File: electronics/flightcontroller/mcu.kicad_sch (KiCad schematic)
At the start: 20 parts, among them J8 Micro_SD_Card_Det_CCON_CTF-11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, J9 SWD, SW1 SW_Push, U3 STM32L462CEUx, U6 GT-24-Mini

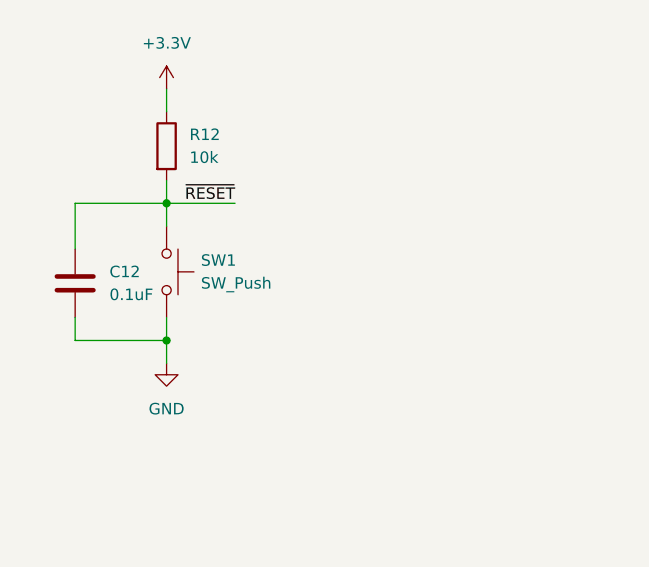
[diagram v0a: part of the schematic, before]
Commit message: electronics: Changed the 4V regulator and added some ordering codes.
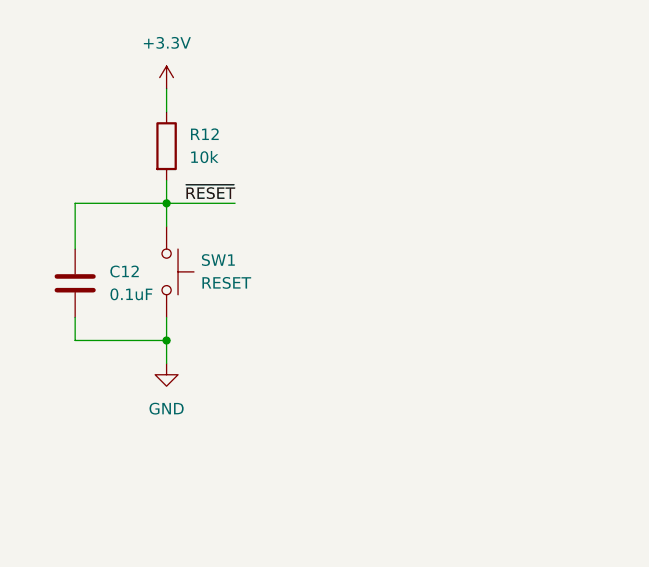
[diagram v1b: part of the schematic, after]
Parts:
- C11, C18, C19: Digikey (none) -> 490-GRM155R60J106ME05DCT-ND
- C12, C13, C14, C15, C16, C17: footprint (none) -> Capacitor_SMD:C_0402_1005Metric; Mouser (none) -> 81-GRM155R61H104KE4D
- SW1: value SW_Push -> RESET; Mouser (none) -> 611-KXT321LHS
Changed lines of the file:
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@@
+      (effects (font (size 1.27 1.27)) hide)
+    )
+    (property "Digikey" "490-GRM155R60J106ME05DCT-ND" (id 4) (at 19.05 179.07 0)
       (effects (font (size 1.27 1.27)) hide)
     )
@@
       (effects (font (size 1.27 1.27)) (justify left))
     )
-    (property "Footprint" "" (id 2) (at 22.5552 48.26 0)
+    (property "Footprint" "Capacitor_SMD:C_0402_1005Metric" (id 2) (at 22.5552 48.26 0)
       (effects (font (size 1.27 1.27)) hide)
     )
     (property "Datasheet" "~" (id 3) (at 21.59 44.45 0)
+      (effects (font (size 1.27 1.27)) hide)
+    )
+    (property "Mouser" "81-GRM155R61H104KE4D" (id 4) (at 21.59 44.45 0)
       (effects (font (size 1.27 1.27)) hide)
     )
@@
       (effects (font (size 1.27 1.27)) (justify left))
     )
-    (property "Footprint" "" (id 2) (at 204.1652 31.75 0)
+    (property "Footprint" "Capacitor_SMD:C_0402_1005Metric" (id 2) (at 204.1652 31.75 0)
       (effects (font (size 1.27 1.27)) hide)
     )
     (property "Datasheet" "~" (id 3) (at 203.2 27.94 0)
+      (effects (font (size 1.27 1.27)) hide)
+    )
+    (property "Mouser" "81-GRM155R61H104KE4D" (id 4) (at 203.2 27.94 0)
       (effects (font (size 1.27 1.27)) hide)
     )
@@
       (effects (font (size 1.27 1.27)) (justify left))
     )
-    (property "Footprint" "" (id 2) (at 216.8652 31.75 0)
+    (property "Footprint" "Capacitor_SMD:C_0402_1005Metric" (id 2) (at 216.8652 31.75 0)
       (effects (font (size 1.27 1.27)) hide)
     )
     (property "Datasheet" "~" (id 3) (at 215.9 27.94 0)
+      (effects (font (size 1.27 1.27)) hide)
+    )
+    (property "Mouser" "81-GRM155R61H104KE4D" (id 4) (at 215.9 27.94 0)
       (effects (font (size 1.27 1.27)) hide)
     )
@@
       (effects (font (size 1.27 1.27)) (justify left))
     )
-    (property "Footprint" "" (id 2) (at 229.5652 31.75 0)
+    (property "Footprint" "Capacitor_SMD:C_0402_1005Metric" (id 2) (at 229.5652 31.75 0)
       (effects (font (size 1.27 1.27)) hide)
     )
     (property "Datasheet" "~" (id 3) (at 228.6 27.94 0)
+      (effects (font (size 1.27 1.27)) hide)
+    )
+    (property "Mouser" "81-GRM155R61H104KE4D" (id 4) (at 228.6 27.94 0)
       (effects (font (size 1.27 1.27)) hide)
     )
@@
       (effects (font (size 1.27 1.27)) (justify left))
     )
-    (property "Footprint" "" (id 2) (at 242.2652 31.75 0)
+    (property "Footprint" "Capacitor_SMD:C_0402_1005Metric" (id 2) (at 242.2652 31.75 0)
       (effects (font (size 1.27 1.27)) hide)
     )
     (property "Datasheet" "~" (id 3) (at 241.3 27.94 0)
+      (effects (font (size 1.27 1.27)) hide)
+    )
+    (property "Mouser" "81-GRM155R61H104KE4D" (id 4) (at 241.3 27.94 0)
       (effects (font (size 1.27 1.27)) hide)
     )
@@
       (effects (font (size 1.27 1.27)) (justify left))
     )
-    (property "Footprint" "" (id 2) (at 254.9652 31.75 0)
+    (property "Footprint" "Capacitor_SMD:C_0402_1005Metric" (id 2) (at 254.9652 31.75 0)
       (effects (font (size 1.27 1.27)) hide)
     )
     (property "Datasheet" "~" (id 3) (at 254 27.94 0)
+      (effects (font (size 1.27 1.27)) hide)
+    )
+    (property "Mouser" "81-GRM155R61H104KE4D" (id 4) (at 254 27.94 0)
       (effects (font (size 1.27 1.27)) hide)
     )
@@
       (effects (font (size 1.27 1.27)) hide)
     )
+    (property "Digikey" "490-GRM155R60J106ME05DCT-ND" (id 4) (at 261.62 118.11 0)
+      (effects (font (size 1.27 1.27)) hide)
+    )
     (pin "1")
     (pin "2")
@@
       (effects (font (size 1.27 1.27)) hide)
     )
+    (property "Digikey" "490-GRM155R60J106ME05DCT-ND" (id 4) (at 266.7 27.94 0)
+      (effects (font (size 1.27 1.27)) hide)
+    )
     (pin "1")
     (pin "2")
@@
       (effects (font (size 1.27 1.27)) (justify left))
     )
-    (property "Value" "SW_Push" (id 1) (at 35.56 44.4499 90)
+    (property "Value" "RESET" (id 1) (at 35.56 44.4499 90)
       (effects (font (size 1.27 1.27)) (justify left))
     )
@@
       (effects (font (size 1.27 1.27)) hide)
     )
+    (property "Mouser" " 611-KXT321LHS" (id 5) (at 31.75 43.18 0)
+      (effects (font (size 1.27 1.27)) hide)
+    )

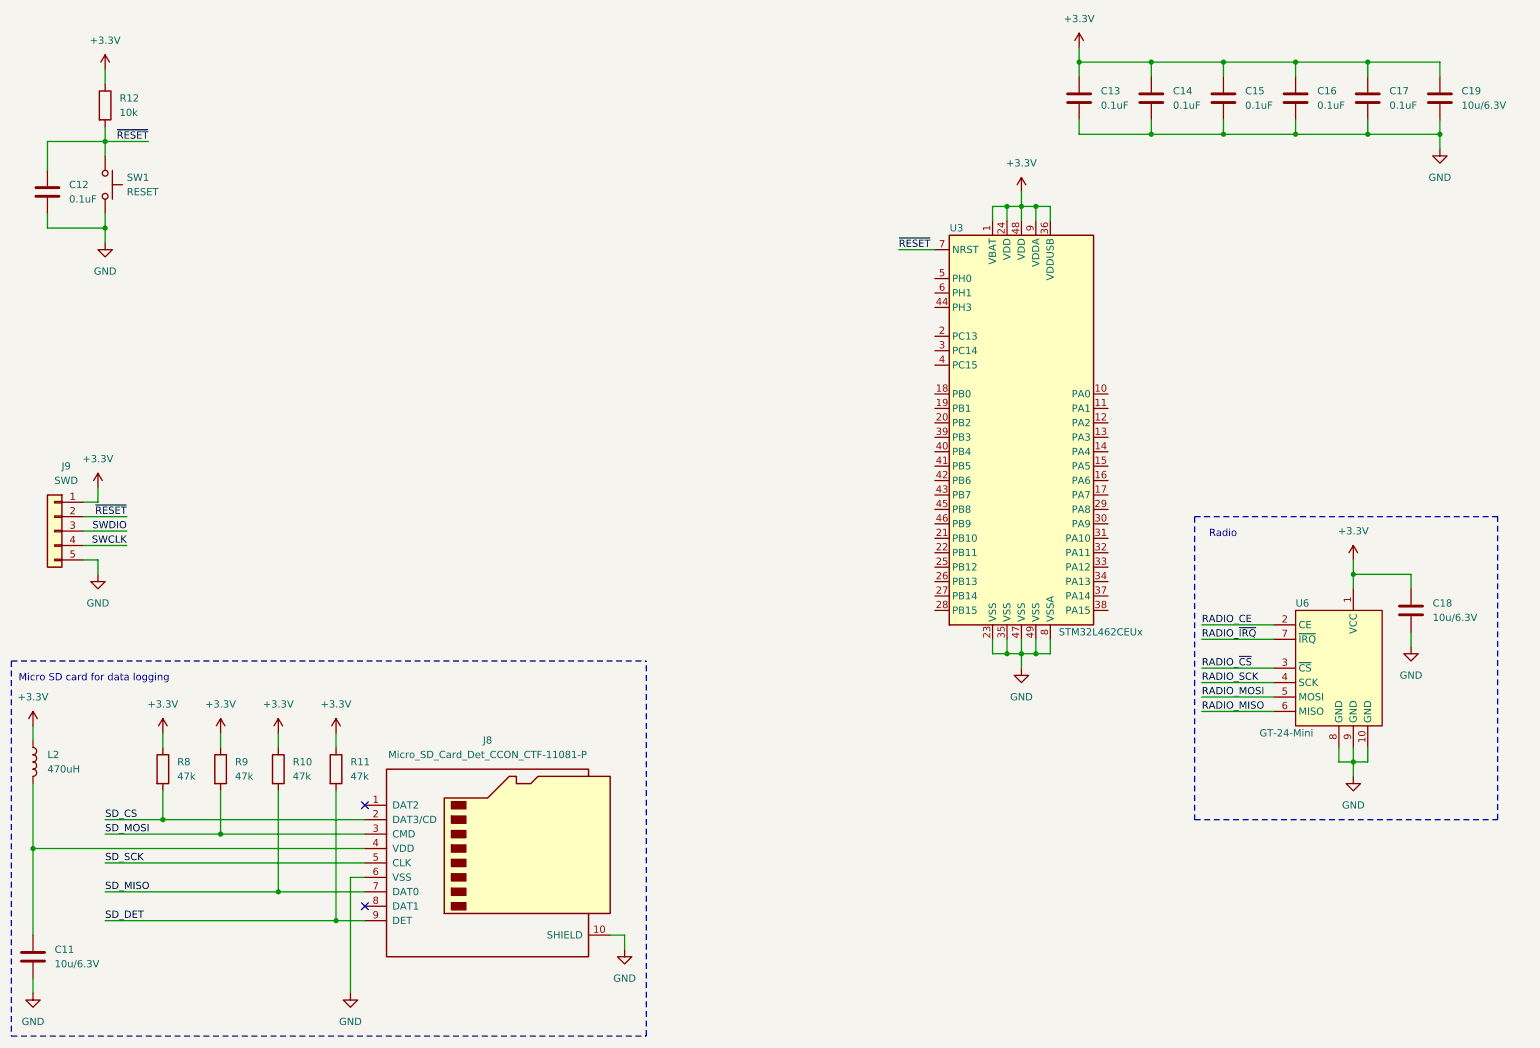
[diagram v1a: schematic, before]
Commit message: PCB: USB, micro SD, and many component changes.
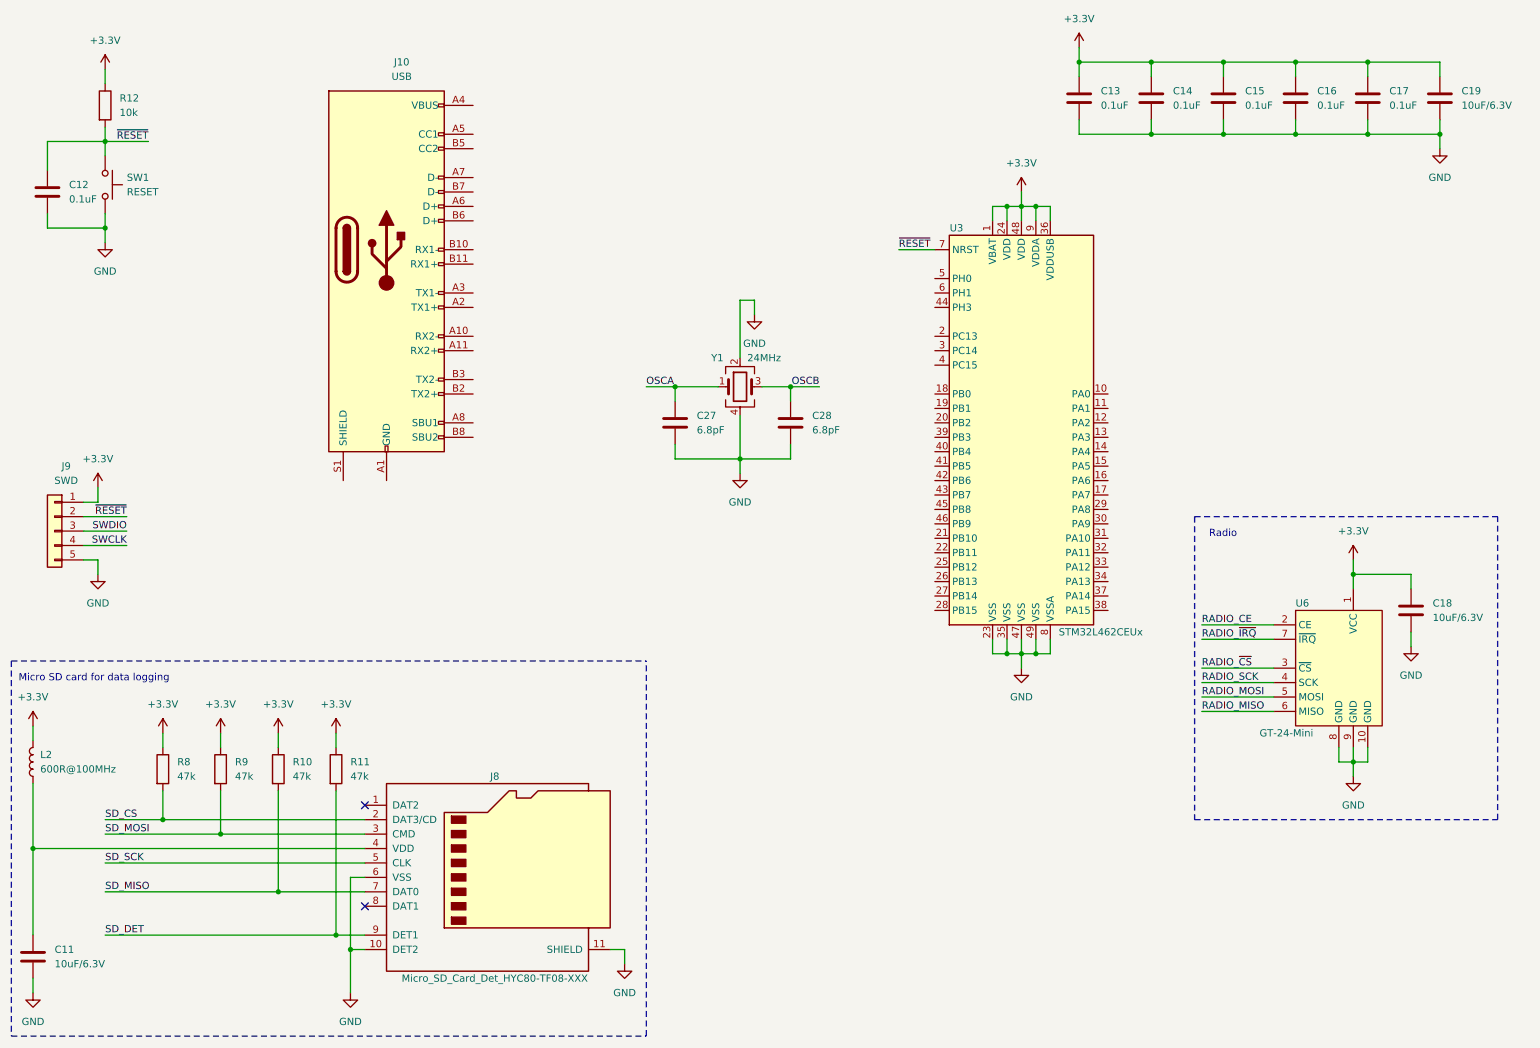
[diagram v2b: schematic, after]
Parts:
- added C27, C28: 6.8pF, Capacitor_SMD:C_0402_1005Metric, symbol Device:C
- added J10: USB, flightcontroller-footprints:USB_C_Receptacle_Amphenol_12402032, symbol Connector:USB_C_Receptacle
- added Y1: 24MHz, Crystal:Crystal_SMD_2016-4Pin_2.0x1.6mm, symbol Device:Crystal_GND24
- C11, C18, C19: value 10u/6.3V -> 10uF/6.3V; footprint (none) -> Capacitor_SMD:C_0402_1005Metric; Digikey 490-GRM155R60J106ME05DCT-ND -> (none); Mouser (none) -> 81-GRM155R60J106M05D
- C12, C13, C14, C15, C16, C17: Mouser 81-GRM155R61H104KE4D -> 81-GRM155R71H104KE4D
- J8: value Micro_SD_Card_Det_CCON_CTF-11081-P -> Micro_SD_Card_Det_HYC80-TF08-XXX; footprint (none) -> flightcontroller-footprints:HYC80-TF08-XXX; symbol flightcontroller-symbols:Micro_SD_Card_Det_CCON_CTF-11081-P -> flightcontroller-symbols:Micro_SD_Card_Det_HYC80-TF08-XXX
- L2: value 470uH -> 600R@100MHz; footprint (none) -> Inductor_SMD:L_0402_1005Metric; Digikey (none) -> 283-MFBM1V1005-501-RCT-ND; Mouser (none) -> 810-MMZ1005S601HT000
- U3: Mouser (none) -> 511-STM32G491CCU6
- U6: footprint (none) -> flightcontroller-footprints:GT-24-Mini
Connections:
- net +3V3: now also L2.2; no longer L2.1
- net GND: now also J8.11 (SHIELD), C27.2, C28.2, Y1.2, Y1.4
- net at C11.1, J8.4 (VDD): now also L2.1; no longer L2.2
- new net: J10.A1 (GND), J10.A12 (GND), J10.B1 (GND), J10.B12 (GND)
- new net: J10.A4 (VBUS), J10.A9 (VBUS), J10.B4 (VBUS), J10.B9 (VBUS)
- new net OSCA: C27.1, Y1.1
- new net OSCB: C28.1, Y1.3

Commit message: electronics: Microcontroller connections, general component placement.
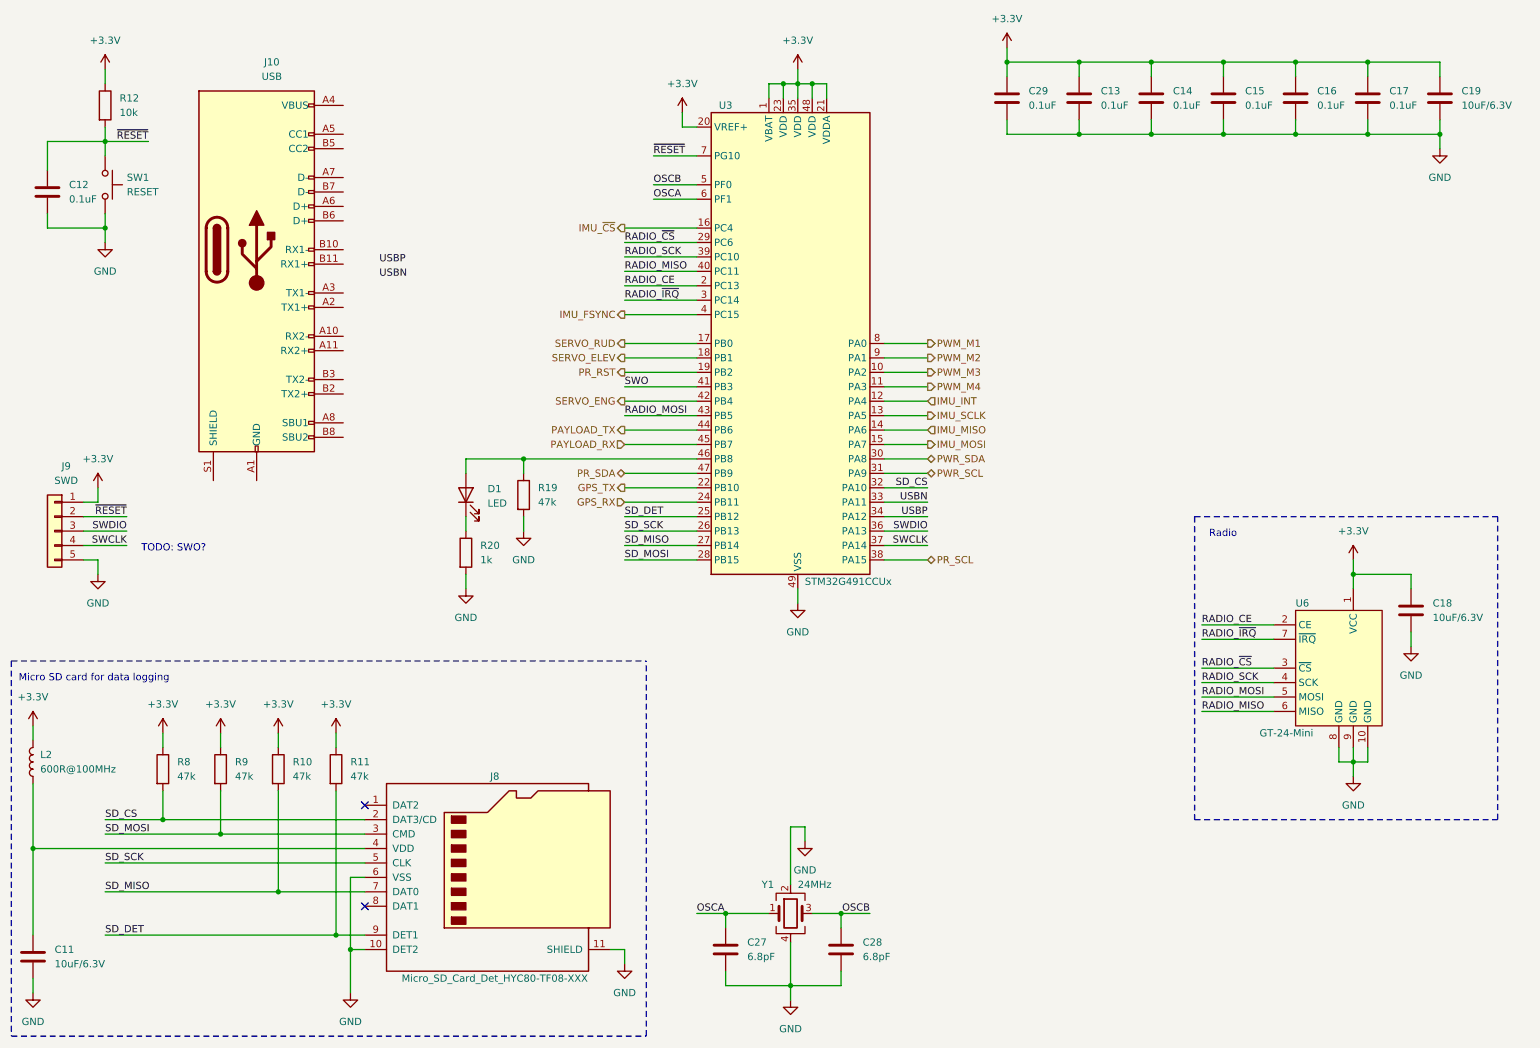
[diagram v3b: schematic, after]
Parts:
- removed U3: STM32L462CEUx, Package_DFN_QFN:QFN-48-1EP_7x7mm_P0.5mm_EP5.6x5.6mm, symbol MCU_ST_STM32L4:STM32L462CEUx
- added C29: 0.1uF, Capacitor_SMD:C_0402_1005Metric, symbol Device:C
- added D1: LED, LED_SMD:LED_0603_1608Metric, symbol Device:LED
- added R19: 47k, Resistor_SMD:R_0402_1005Metric, symbol Device:R
- added R20: 1k, Resistor_SMD:R_0402_1005Metric, symbol Device:R
- added U3: STM32G491CCUx, Package_DFN_QFN:QFN-48-1EP_7x7mm_P0.5mm_EP5.6x5.6mm, symbol flightcontroller-symbols:STM32G491CCUx
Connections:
- net +3V3: now also C29.1, U3.1 (VBAT), U3.20 (VREF+), U3.21 (VDDA), U3.23 (VDD), U3.35 (VDD), U3.48 (VDD)
- net GND: now also C29.2, R19.2, R20.2, U3.49 (VSS)
- net OSCA: now also U3.6 (PF1)
- net OSCB: now also U3.5 (PF0)
- net RADIO_CE: now also U3.2 (PC13)
- net RADIO_MISO: now also U3.40 (PC11)
- net RADIO_MOSI: now also U3.43 (PB5)
- net RADIO_SCK: now also U3.39 (PC10)
- net RADIO_~{CS}: now also U3.29 (PC6)
- net RADIO_~{IRQ}: now also U3.3 (PC14)
- net SD_CS: now also U3.32 (PA10)
- net SD_DET: now also U3.25 (PB12)
- net SD_MISO: now also U3.27 (PB14)
- net SD_MOSI: now also U3.28 (PB15)
- net SD_SCK: now also U3.26 (PB13)
- net SWCLK: now also U3.37 (PA14)
- net SWDIO: now also U3.36 (PA13)
- net ~{RESET}: now also U3.7 (PG10)
- new net: D1.2 (A), R19.1, U3.46 (PB8)
- new net: D1.1 (K), R20.1
- new net GPS_RX: U3.24 (PB11)
- new net GPS_TX: U3.22 (PB10)
- new net IMU_FSYNC: U3.4 (PC15)
- new net IMU_INT: U3.12 (PA4)
- new net IMU_MISO: U3.14 (PA6)
- new net IMU_MOSI: U3.15 (PA7)
- new net IMU_SCLK: U3.13 (PA5)
- new net IMU_~{CS}: U3.16 (PC4)
- new net PAYLOAD_RX: U3.45 (PB7)
- new net PAYLOAD_TX: U3.44 (PB6)
- new net PR_RST: U3.19 (PB2)
- new net PR_SCL: U3.38 (PA15)
- new net PR_SDA: U3.47 (PB9)
- new net PWM_M1: U3.8 (PA0)
- new net PWM_M2: U3.9 (PA1)
- new net PWM_M3: U3.10 (PA2)
- new net PWM_M4: U3.11 (PA3)
- new net PWR_SCL: U3.31 (PA9)
- new net PWR_SDA: U3.30 (PA8)
- new net SERVO_ELEV: U3.18 (PB1)
- new net SERVO_ENG: U3.42 (PB4)
- new net SERVO_RUD: U3.17 (PB0)
- new net SWO: U3.41 (PB3)
- new net USBN: U3.33 (PA11)
- new net USBP: U3.34 (PA12)
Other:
- note added: "TODO: SWO?"
- moved on the sheet: C27, C28, J10, Y1
